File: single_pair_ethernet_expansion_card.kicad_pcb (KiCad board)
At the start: 4 copper layers, 26 x 30 mm, 55 parts, among them IC1 DP83TC813RRHFRQ1, J1 Conn_01x02, P1 USB_C_Plug, U1 LAN7801_9JX, U2 LP38693SD-3.3, U3 HD3SS3220IRNHT, U4 KC2520Z125.000C1KX00, U5 KC2520Z25.0000C1KX00

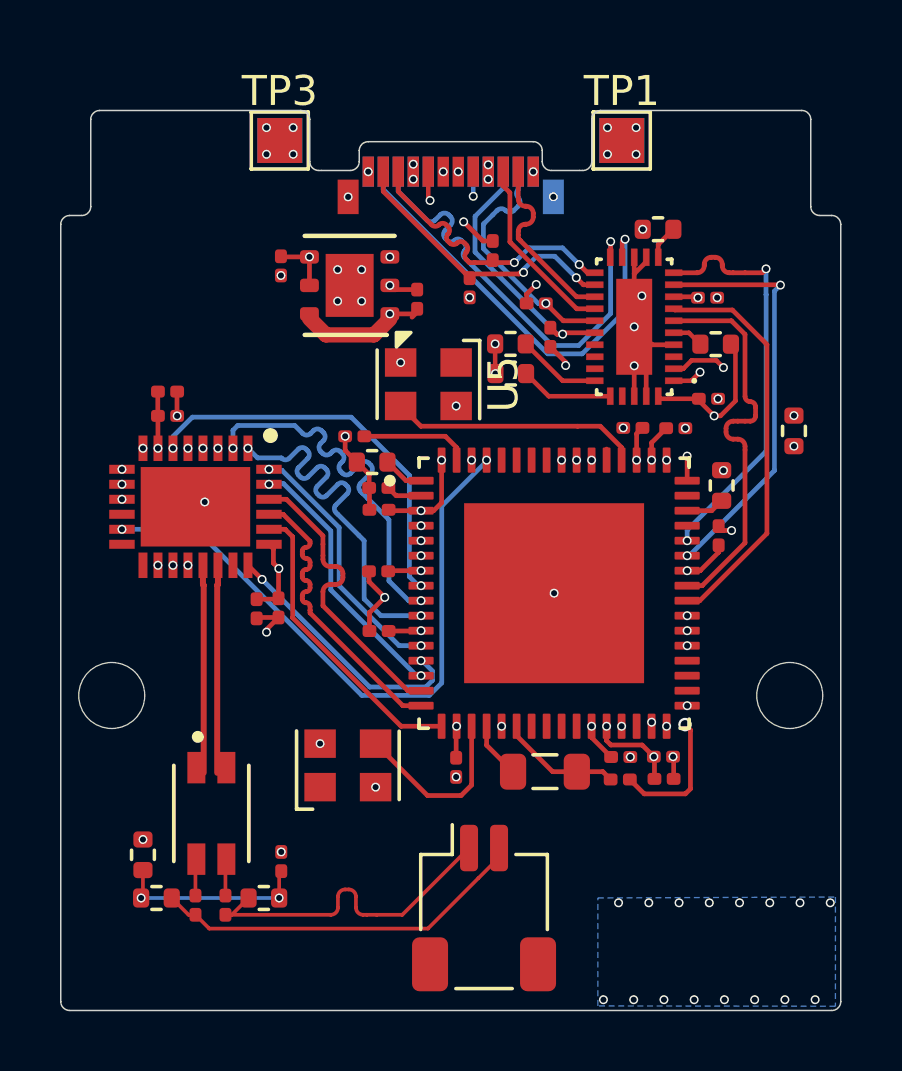
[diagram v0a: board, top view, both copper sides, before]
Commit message: fixed impedence
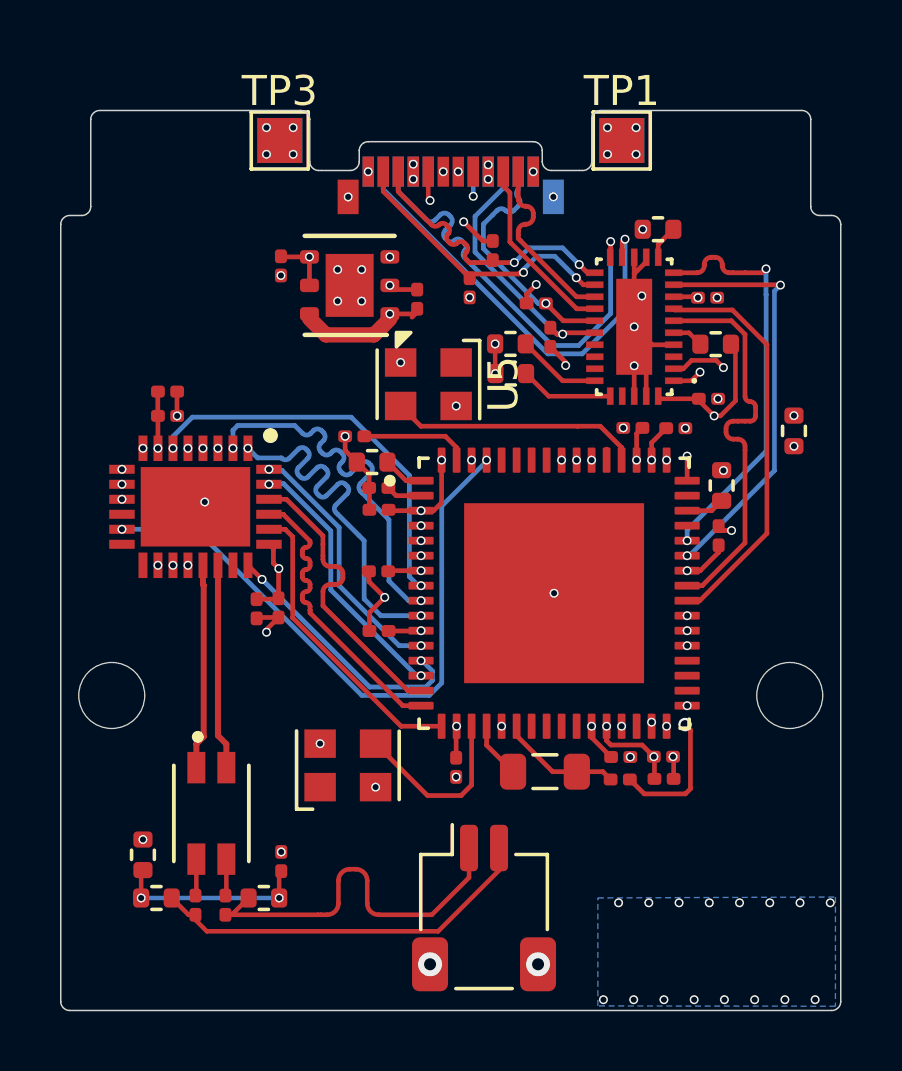
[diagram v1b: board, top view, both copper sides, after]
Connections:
- J1 pad MP: (no net) -> GND
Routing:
- net Net-(J1-Pin_1): track 11.1 -> 12.9 mm
- net Net-(J1-Pin_2): track 12.3 -> 13.1 mm
- net GND: vias 61 -> 63
